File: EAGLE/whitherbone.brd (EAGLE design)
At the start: 86.4 x 54.6 mm, 215 parts, among them IC1 A4983, IC12 TPS2051BDGN, IC13 SN74AUC1G74, IC14 TPD4S012DRY, IC15 TPD4S012DRY, IC17 SN74LVC2G241DCUR, IC2 SN74LVC1G07DCK, IC4 7805T, IC7 IP4283CZ10-TBR, IC8 IP4283CZ10-TBR, IC9 TDA19988BHN/C1,557, J1 1-1747981-1, Q2 32.768kHz, Q4 24 MHz, T1 BSS138W-7-F, T3 BSS138W-7-F, T4 BSS138W-7-F, U1 OSD3358-512M-BSM, X2 SCHA5B0200, X4 10118192-0001LF

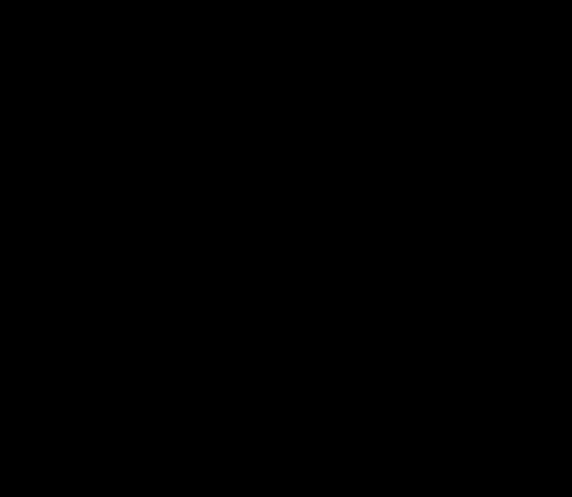
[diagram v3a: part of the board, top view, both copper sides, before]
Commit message: Wired up BigEasyDriver
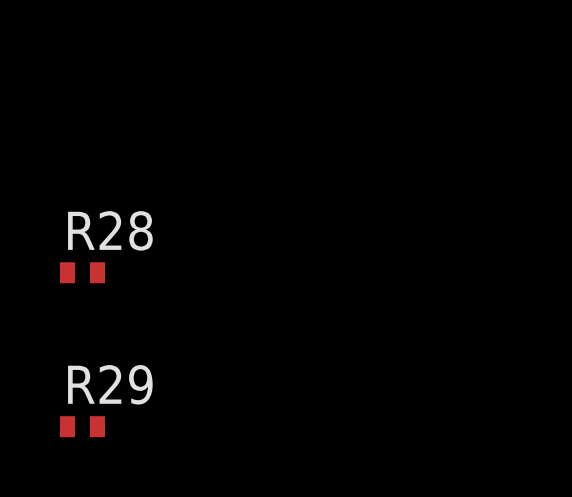
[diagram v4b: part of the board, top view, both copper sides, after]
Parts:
- added R28: 47k, 1%, rcl:R0402
- added R29: 22k, 1%, rcl:R0402
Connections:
- removed net DIR: IC1.P$19, R22.1
- removed net ENABLE: IC1.P$2, R21.1
- removed net MS1: IC1.P$9, R11.1
- removed net MS2: IC1.P$10, R12.1
- removed net MS3: IC1.P$11, R13.1
- removed net RESET: IC1.P$12, R15.1
- removed net SLEEP: IC1.P$14, R14.1
- removed net STEP: IC1.P$16, R23.1
- new net DIR(GPIO23): IC1.P$19, R22.1, U1.P5
- new net ENABLE(GPIO46): IC1.P$2, R21.1, U1.T6
- new net MS1(GPIO27): IC1.P$9, R11.1, U1.T5
- new net MS2(GPIO44): IC1.P$10, R12.1, U1.P6
- new net MS3(GPIO45): IC1.P$11, R13.1, U1.R6
- new net N$49: R28.1, R29.1, U1.A8
- new net RESET(GPIO26): IC1.P$12, R15.1, U1.R5
- new net SLEEP(GPIO47): IC1.P$14, R14.1, U1.P7
- new net STEP(GPIO22): IC1.P$16, R23.1, U1.T4
- net CUR_REF: now also R28.2
- net GND: now also R29.2
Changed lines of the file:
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@@
 <element name="JP3" library="SparkFun" package="1X04" value="" x="-52.3494" y="-192.9892"/>
 <element name="JP5" library="BigEasyDriver_v11" package="SCREWTERMINAL-3.5MM-4_LOCK" value="" x="-51.4096" y="-173.4312"/>
+<element name="R28" library="rcl" package="R0402" value="47k, 1%" x="-60.6044" y="-204.978"/>
+<element name="R29" library="rcl" package="R0402" value="22k, 1%" x="-60.6044" y="-210.1088"/>
 </elements>
 <signals>
@@
 <contactref element="C15" pad="2"/>
 <contactref element="R21" pad="2"/>
+<contactref element="R29" pad="2"/>
 <wire x1="-53.2996" y1="-153.3144" x2="-56.3984" y2="-153.3144" width="0" layer="19" extent="1-1"/>
 <wire x1="-50.2008" y1="-153.3144" x2="-53.2996" y2="-153.3144" width="0" layer="19" extent="1-1"/>
@@
 <wire x1="-42.9162" y1="-145.0848" x2="-49.9266" y2="-145.0848" width="0" layer="19" extent="1-1"/>
 <wire x1="-33.8464" y1="-144.0202" x2="-42.9162" y2="-145.0848" width="0" layer="19" extent="1-1"/>
+<wire x1="-60.1044" y1="-210.1088" x2="-53.2996" y2="-156.4894" width="0" layer="19" extent="1-1"/>
 <wire x1="-46.857" y1="-85.0646" x2="-49.9266" y2="-145.0848" width="0" layer="19" extent="1-1"/>
 <wire x1="-30.211" y1="-72.9844" x2="-46.857" y2="-85.0646" width="0" layer="19" extent="1-1"/>
@@
 <contactref element="TP2" pad="TP"/>
 <contactref element="IC1" pad="P$17"/>
+<contactref element="R28" pad="2"/>
 <wire x1="-50.9524" y1="-129.7686" x2="-54.0896" y2="-146.7024" width="0" layer="19" extent="1-1"/>
 <wire x1="-34.6964" y1="-141.1202" x2="-50.9524" y2="-129.7686" width="0" layer="19" extent="1-1"/>
+<wire x1="-60.1044" y1="-204.978" x2="-54.0896" y2="-146.7024" width="0" layer="19" extent="1-1"/>
 </signal>
 <signal name="COILB+">
@@
 <wire x1="-56.9896" y1="-143.8024" x2="-47.7318" y2="-173.4312" width="0" layer="19" extent="1-1"/>
 </signal>
-<signal name="DIR">
+<signal name="DIR(GPIO23)">
 <contactref element="IC1" pad="P$19"/>
 <contactref element="R22" pad="1"/>
+<contactref element="U1" pad="P5"/>
 <wire x1="-54.0896" y1="-145.7024" x2="-48.402" y2="-156.4894" width="0" layer="19" extent="1-1"/>
+<wire x1="59.4868" y1="66.1416" x2="-54.0896" y2="-145.7024" width="0" layer="19" extent="1-1"/>
 </signal>
-<signal name="MS1">
+<signal name="MS1(GPIO27)">
 <contactref element="IC1" pad="P$9"/>
 <contactref element="R11" pad="1"/>
+<contactref element="U1" pad="T5"/>
 <wire x1="-42.2044" y1="-153.3144" x2="-57.4896" y2="-148.6024" width="0" layer="19" extent="1-1"/>
+<wire x1="62.0268" y1="66.1416" x2="-42.2044" y2="-153.3144" width="0" layer="19" extent="1-1"/>
 </signal>
-<signal name="MS2">
+<signal name="MS2(GPIO44)">
 <contactref element="IC1" pad="P$10"/>
 <contactref element="R12" pad="1"/>
+<contactref element="U1" pad="P6"/>
 <wire x1="-39.1056" y1="-153.3144" x2="-56.9896" y2="-148.6024" width="0" layer="19" extent="1-1"/>
+<wire x1="59.4868" y1="67.4116" x2="-39.1056" y2="-153.3144" width="0" layer="19" extent="1-1"/>
 </signal>
-<signal name="ENABLE">
+<signal name="ENABLE(GPIO46)">
 <contactref element="IC1" pad="P$2"/>
 <contactref element="R21" pad="1"/>
+<contactref element="U1" pad="T6"/>
 <wire x1="-58.8896" y1="-145.2024" x2="-51.5008" y2="-156.4894" width="0" layer="19" extent="1-1"/>
+<wire x1="62.0268" y1="67.4116" x2="-58.8896" y2="-145.2024" width="0" layer="19" extent="1-1"/>
 </signal>
 <signal name="COILA-">
@@
 <wire x1="-54.0896" y1="-144.7024" x2="-40.7318" y2="-173.4312" width="0" layer="19" extent="1-1"/>
 </signal>
-<signal name="RESET">
+<signal name="RESET(GPIO26)">
 <contactref element="IC1" pad="P$12"/>
 <contactref element="R15" pad="1"/>
+<contactref element="U1" pad="R5"/>
 <wire x1="-55.9896" y1="-148.6024" x2="-57.6984" y2="-156.4894" width="0" layer="19" extent="1-1"/>
+<wire x1="60.7568" y1="66.1416" x2="-55.9896" y2="-148.6024" width="0" layer="19" extent="1-1"/>
 </signal>
-<signal name="STEP">
+<signal name="STEP(GPIO22)">
 <contactref element="IC1" pad="P$16"/>
 <contactref element="R23" pad="1"/>
+<contactref element="U1" pad="T4"/>
 <wire x1="-45.3032" y1="-156.4894" x2="-54.0896" y2="-147.2024" width="0" layer="19" extent="1-1"/>
+<wire x1="62.0268" y1="64.8716" x2="-54.0896" y2="-147.2024" width="0" layer="19" extent="1-1"/>
 </signal>
-<signal name="SLEEP">
+<signal name="SLEEP(GPIO47)">
 <contactref element="IC1" pad="P$14"/>
 <contactref element="R14" pad="1"/>
+<contactref element="U1" pad="P7"/>
 <wire x1="-54.9896" y1="-148.6024" x2="-60.7972" y2="-156.4894" width="0" layer="19" extent="1-1"/>
+<wire x1="59.4868" y1="68.6816" x2="-54.9896" y2="-148.6024" width="0" layer="19" extent="1-1"/>
 </signal>
 <signal name="N$31">
@@
 <wire x1="-45.3032" y1="-153.3144" x2="-58.8896" y2="-147.2024" width="0" layer="19" extent="1-1"/>
 </signal>
-<signal name="MS3">
+<signal name="MS3(GPIO45)">
 <contactref element="IC1" pad="P$11"/>
 <contactref element="R13" pad="1"/>
+<contactref element="U1" pad="R6"/>
 <wire x1="-36.0068" y1="-153.3144" x2="-56.4896" y2="-148.6024" width="0" layer="19" extent="1-1"/>
+<wire x1="60.7568" y1="67.4116" x2="-36.0068" y2="-153.3144" width="0" layer="19" extent="1-1"/>
 </signal>
 <signal name="N$48">
@@
 <wire x1="-35.5464" y1="-144.0202" x2="-40.9044" y2="-156.4894" width="0" layer="19" extent="1-1"/>
 </signal>
+<signal name="N$49">
+<contactref element="U1" pad="A8"/>
+<contactref element="R28" pad="1"/>
+<contactref element="R29" pad="1"/>
+<wire x1="-61.1044" y1="-204.978" x2="42.9768" y2="69.9516" width="0" layer="19" extent="1-1"/>
+<wire x1="-61.1044" y1="-210.1088" x2="-61.1044" y2="-204.978" width="0" layer="19" extent="1-1"/>
+</signal>
 </signals>

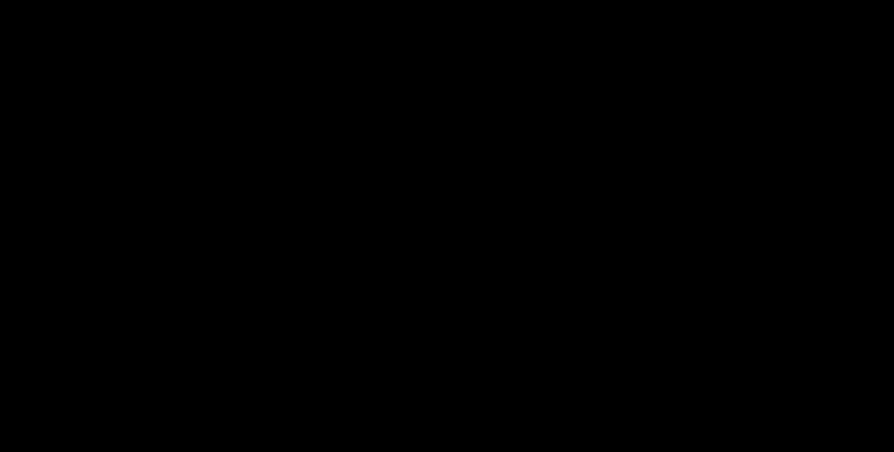
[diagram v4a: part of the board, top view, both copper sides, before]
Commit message: Add connector for Neopixels (not yet connected)
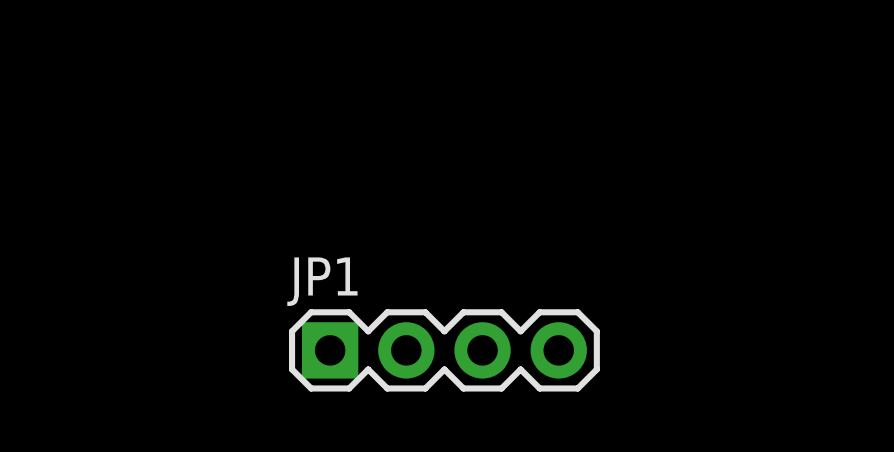
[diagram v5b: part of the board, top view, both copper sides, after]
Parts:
- added JP1: (no value), SparkFun:1X04
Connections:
- new net TO_NEOPIXEL: U1.B2
- net GND: now also JP1.1
- net VDD_5V: now also JP1.4
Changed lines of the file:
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@@
 <element name="R28" library="rcl" package="R0402" value="47k, 1%" x="-60.6044" y="-204.978"/>
 <element name="R29" library="rcl" package="R0402" value="22k, 1%" x="-60.6044" y="-210.1088"/>
+<element name="JP1" library="SparkFun" package="1X04" value="" x="-52.3494" y="-242.3668"/>
 </elements>
 <signals>
@@
 <contactref element="R21" pad="2"/>
 <contactref element="R29" pad="2"/>
+<contactref element="JP1" pad="1"/>
 <wire x1="-53.2996" y1="-153.3144" x2="-56.3984" y2="-153.3144" width="0" layer="19" extent="1-1"/>
 <wire x1="-50.2008" y1="-153.3144" x2="-53.2996" y2="-153.3144" width="0" layer="19" extent="1-1"/>
@@
 <wire x1="-33.8464" y1="-144.0202" x2="-42.9162" y2="-145.0848" width="0" layer="19" extent="1-1"/>
 <wire x1="-60.1044" y1="-210.1088" x2="-53.2996" y2="-156.4894" width="0" layer="19" extent="1-1"/>
+<wire x1="-52.3494" y1="-242.3668" x2="-60.1044" y2="-210.1088" width="0" layer="19" extent="1-1"/>
 <wire x1="-46.857" y1="-85.0646" x2="-49.9266" y2="-145.0848" width="0" layer="19" extent="1-1"/>
 <wire x1="-30.211" y1="-72.9844" x2="-46.857" y2="-85.0646" width="0" layer="19" extent="1-1"/>
@@
 <contactref element="U1" pad="R10"/>
 <contactref element="U1" pad="T10"/>
+<contactref element="JP1" pad="4"/>
 <wire x1="60.7568" y1="72.4916" x2="62.0268" y2="72.4916" width="0" layer="19" extent="1-1"/>
 <wire x1="59.4868" y1="72.4916" x2="60.7568" y2="72.4916" width="0" layer="19" extent="1-1"/>
 <wire x1="-24.6888" y1="-39.2176" x2="59.4868" y2="72.4916" width="0" layer="19" extent="1-1"/>
+<wire x1="-44.7294" y1="-242.3668" x2="-24.6888" y2="-39.2176" width="0" layer="19" extent="1-1"/>
 </signal>
 <signal name="PWR_BUT">
@@
 <wire x1="-61.1044" y1="-210.1088" x2="-61.1044" y2="-204.978" width="0" layer="19" extent="1-1"/>
 </signal>
+<signal name="TO_NEOPIXEL">
+<contactref element="U1" pad="B2"/>
+</signal>
 </signals>

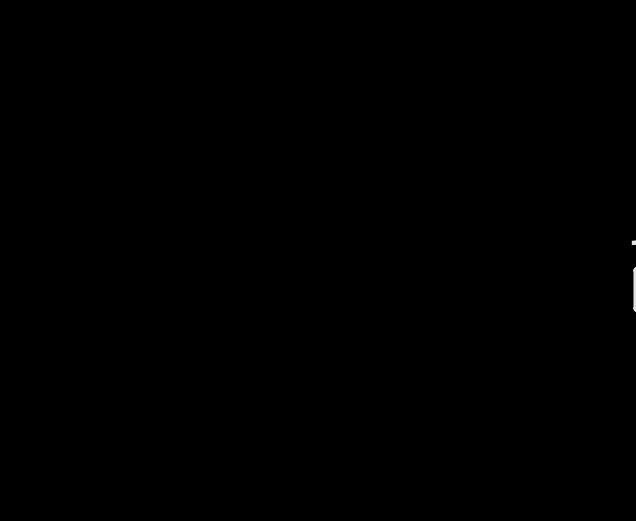
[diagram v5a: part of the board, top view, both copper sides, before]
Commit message: Connected NEOPIXEL connector
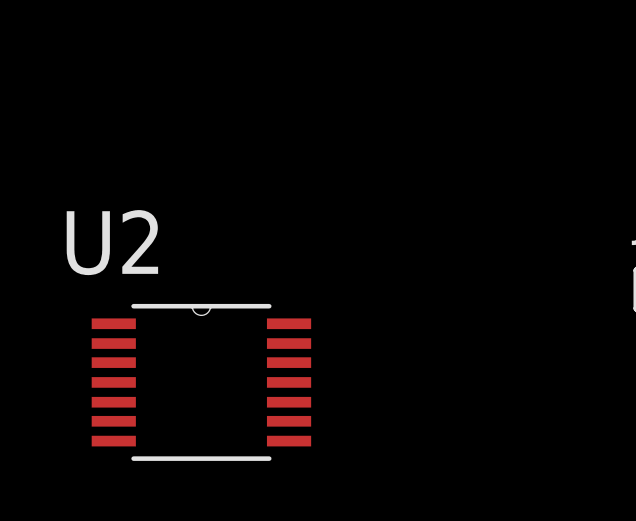
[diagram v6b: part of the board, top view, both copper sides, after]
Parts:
- added U2: SN74AHCT125PW, SN74AHCT125PW:SOP65P640X120-14N
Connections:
- new net N$51: JP1.3, U2.3
- net GND: now also U2.1, U2.12, U2.5, U2.7, U2.9
- net TO_NEOPIXEL: now also U2.2
- net VDD_5V: now also U2.10, U2.13, U2.14, U2.4
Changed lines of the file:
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@@
 <element name="R29" library="rcl" package="R0402" value="22k, 1%" x="-60.6044" y="-210.1088"/>
 <element name="JP1" library="SparkFun" package="1X04" value="" x="-52.3494" y="-242.3668"/>
+<element name="U2" library="SN74AHCT125PW" package="SOP65P640X120-14N" value="SN74AHCT125PW" x="-68.1228" y="-245.4656">
+<attribute name="DESCRIPTION" value=" Quadruple Bus Buffer Gates With 3-State Outputs 14-TSSOP -40 to 125 " x="-68.1228" y="-245.4656" size="1.778" layer="27" display="off"/>
+<attribute name="DIGI-KEY_PART_NUMBER" value="296-26414-5-ND" x="-68.1228" y="-245.4656" size="1.778" layer="27" display="off"/>
+<attribute name="DIGI-KEY_PURCHASE_URL" value="https://www.digikey.com/product-detail/en/texas-instruments/SN74AHCT125PW/296-26414-5-ND/1567014?utm_source=snapeda&amp;utm_medium=aggregator&amp;utm_campaign=symbol" x="-68.1228" y="-245.4656" size="1.778" layer="27" display="off"/>
+<attribute name="MF" value="Texas Instruments" x="-68.1228" y="-245.4656" size="1.778" layer="27" display="off"/>
+<attribute name="MP" value="SN74AHCT125PW" x="-68.1228" y="-245.4656" size="1.778" layer="27" display="off"/>
+<attribute name="PACKAGE" value="TSSOP-14 Texas Instruments" x="-68.1228" y="-245.4656" size="1.778" layer="27" display="off"/>
+</element>
 </elements>
 <signals>
@@
 <contactref element="R29" pad="2"/>
 <contactref element="JP1" pad="1"/>
+<contactref element="U2" pad="7"/>
+<contactref element="U2" pad="1"/>
+<contactref element="U2" pad="5"/>
+<contactref element="U2" pad="9"/>
+<contactref element="U2" pad="12"/>
 <wire x1="-53.2996" y1="-153.3144" x2="-56.3984" y2="-153.3144" width="0" layer="19" extent="1-1"/>
 <wire x1="-50.2008" y1="-153.3144" x2="-53.2996" y2="-153.3144" width="0" layer="19" extent="1-1"/>
@@
 <wire x1="-60.1044" y1="-210.1088" x2="-53.2996" y2="-156.4894" width="0" layer="19" extent="1-1"/>
 <wire x1="-52.3494" y1="-242.3668" x2="-60.1044" y2="-210.1088" width="0" layer="19" extent="1-1"/>
+<wire x1="-65.2018" y1="-244.8052" x2="-52.3494" y2="-242.3668" width="0" layer="19" extent="1-1"/>
+<wire x1="-65.2018" y1="-246.761" x2="-65.2018" y2="-244.8052" width="0" layer="19" extent="1-1"/>
+<wire x1="-71.0438" y1="-247.4214" x2="-65.2018" y2="-246.761" width="0" layer="19" extent="1-1"/>
+<wire x1="-71.0438" y1="-246.126" x2="-71.0438" y2="-247.4214" width="0" layer="19" extent="1-1"/>
+<wire x1="-71.0438" y1="-243.5098" x2="-71.0438" y2="-246.126" width="0" layer="19" extent="1-1"/>
 <wire x1="-46.857" y1="-85.0646" x2="-49.9266" y2="-145.0848" width="0" layer="19" extent="1-1"/>
 <wire x1="-30.211" y1="-72.9844" x2="-46.857" y2="-85.0646" width="0" layer="19" extent="1-1"/>
@@
 <contactref element="U1" pad="T10"/>
 <contactref element="JP1" pad="4"/>
+<contactref element="U2" pad="14"/>
+<contactref element="U2" pad="4"/>
+<contactref element="U2" pad="10"/>
+<contactref element="U2" pad="13"/>
 <wire x1="60.7568" y1="72.4916" x2="62.0268" y2="72.4916" width="0" layer="19" extent="1-1"/>
 <wire x1="59.4868" y1="72.4916" x2="60.7568" y2="72.4916" width="0" layer="19" extent="1-1"/>
 <wire x1="-24.6888" y1="-39.2176" x2="59.4868" y2="72.4916" width="0" layer="19" extent="1-1"/>
 <wire x1="-44.7294" y1="-242.3668" x2="-24.6888" y2="-39.2176" width="0" layer="19" extent="1-1"/>
+<wire x1="-65.2018" y1="-243.5098" x2="-44.7294" y2="-242.3668" width="0" layer="19" extent="1-1"/>
+<wire x1="-65.2018" y1="-244.1702" x2="-65.2018" y2="-243.5098" width="0" layer="19" extent="1-1"/>
+<wire x1="-65.2018" y1="-246.126" x2="-65.2018" y2="-244.1702" width="0" layer="19" extent="1-1"/>
+<wire x1="-71.0438" y1="-245.4656" x2="-65.2018" y2="-246.126" width="0" layer="19" extent="1-1"/>
 </signal>
 <signal name="PWR_BUT">
@@
 <signal name="TO_NEOPIXEL">
 <contactref element="U1" pad="B2"/>
+<contactref element="U2" pad="2"/>
+<wire x1="-71.0438" y1="-244.1702" x2="44.2468" y2="62.3316" width="0" layer="19" extent="1-1"/>
+</signal>
+<signal name="N$51">
+<contactref element="JP1" pad="3"/>
+<contactref element="U2" pad="3"/>
+<wire x1="-47.2694" y1="-242.3668" x2="-71.0438" y2="-244.8052" width="0" layer="19" extent="1-1"/>
 </signal>
 </signals>

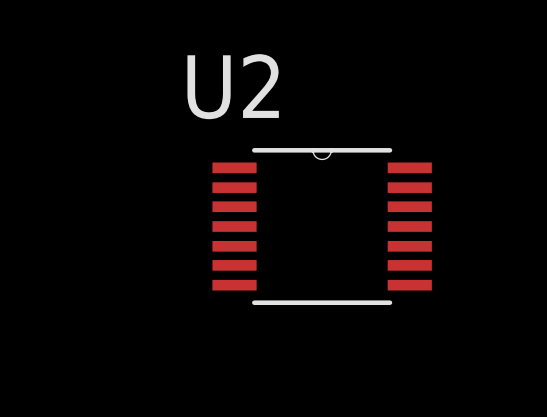
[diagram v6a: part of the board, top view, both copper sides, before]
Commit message: Add quick decoupling cap for neopixel output
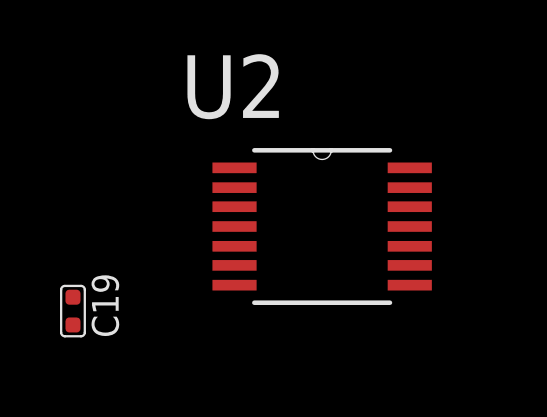
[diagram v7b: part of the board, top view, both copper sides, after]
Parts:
- added C19: 1uF,10V, Seeed-Capacitor:C0402
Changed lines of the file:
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@@
 <attribute name="PACKAGE" value="TSSOP-14 Texas Instruments" x="-68.1228" y="-245.4656" size="1.778" layer="27" display="off"/>
+</element>
+<element name="C19" library="Seeed-Capacitor" package="C0402" value="1uF,10V" x="-76.4286" y="-248.285">
+<attribute name="MPN" value="CC0402KRX5R6BB105" x="-76.4286" y="-248.285" size="1.778" layer="27" display="off"/>
 </element>
 </elements>
